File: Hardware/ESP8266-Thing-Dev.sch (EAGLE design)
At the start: 83 parts, among them J1 DNP, Q1 MMBT2222A, Q2 MMBT2222A, Q4 BSS138, Q5 BSS138, Q6 BSS138, Q7 BSS138, Q8 BSS138, U1 AP2112K-3.3V, U2 ESP8266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

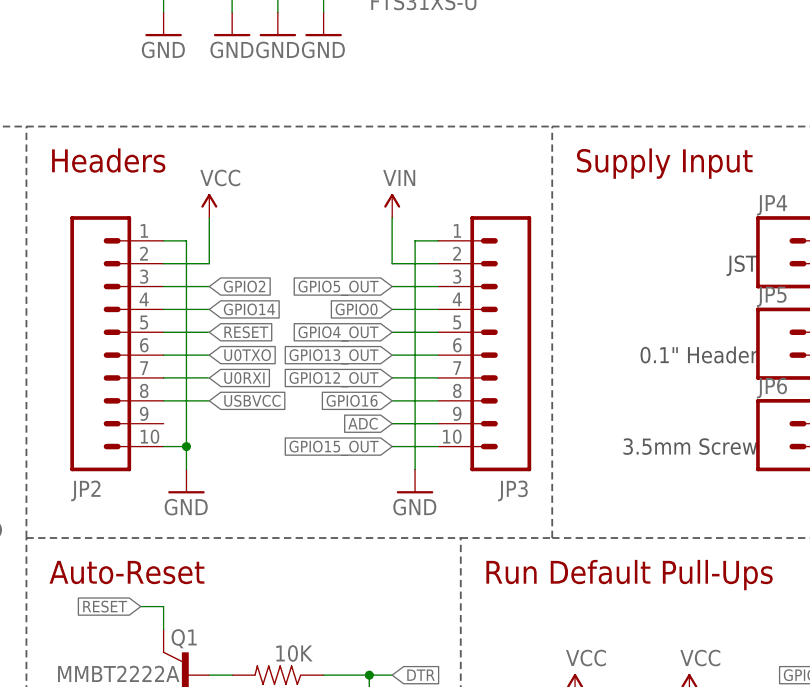
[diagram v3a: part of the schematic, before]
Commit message: Switch to 7 pin header. Make board outline larger.
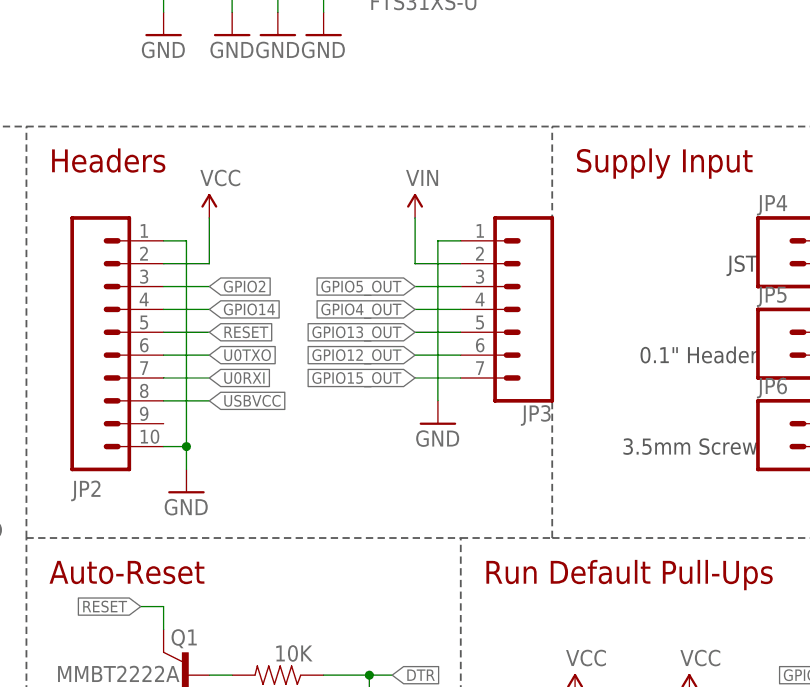
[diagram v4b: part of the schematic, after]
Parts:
- JP3: device SparkFun-Connectors:M10NO_SILK_PTH_FEMALE -> SparkFun-Connectors:CONN_07NO_SILK
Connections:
- net ADC: no longer JP3.9
- net GPIO0: no longer JP3.4
- net GPIO12_OUT: now also JP3.6; no longer JP3.7
- net GPIO13_OUT: now also JP3.5; no longer JP3.6
- net GPIO15_OUT: now also JP3.7; no longer JP3.10
- net GPIO16: no longer JP3.8
- net GPIO4_OUT: now also JP3.4; no longer JP3.5
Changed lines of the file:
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@@
 <layer number="112" name="tSilk" color="7" fill="1" visible="yes" active="yes"/>
 <layer number="113" name="IDFDebug" color="4" fill="1" visible="yes" active="yes"/>
+<layer number="114" name="Badge_Outline" color="7" fill="1" visible="yes" active="yes"/>
+<layer number="115" name="ReferenceISLANDS" color="7" fill="1" visible="yes" active="yes"/>
 <layer number="116" name="Patch_BOT" color="9" fill="4" visible="yes" active="yes"/>
 <layer number="118" name="Rect_Pads" color="7" fill="1" visible="yes" active="yes"/>
@@
 <layer number="230" name="230bmp" color="7" fill="1" visible="yes" active="yes"/>
 <layer number="231" name="231bmp" color="7" fill="1" visible="yes" active="yes"/>
+<layer number="232" name="Eagle3D_PG2" color="7" fill="1" visible="yes" active="yes"/>
+<layer number="233" name="Eagle3D_PG3" color="7" fill="1" visible="yes" active="yes"/>
 <layer number="248" name="Housing" color="7" fill="1" visible="yes" active="yes"/>
 <layer number="249" name="Edge" color="7" fill="1" visible="yes" active="yes"/>
@@
 <part name="SJ2" library="SparkFun-Passives" deviceset="JUMPER-PTH-2-NO" device="" value="SLEEP-PTH"/>
 <part name="JP2" library="SparkFun-Connectors" deviceset="M10" device="NO_SILK_PTH_FEMALE"/>
-<part name="JP3" library="SparkFun-Connectors" deviceset="M10" device="NO_SILK_PTH_FEMALE"/>
 <part name="STANDOFF3" library="SparkFun-Electromechanical" deviceset="STAND-OFF" device=""/>
 <part name="STANDOFF1" library="SparkFun-Electromechanical" deviceset="STAND-OFF" device=""/>
@@
 <part name="R28" library="SparkFun" deviceset="RESISTOR" device="0603-RES" value="10K"/>
 <part name="R29" library="SparkFun" deviceset="RESISTOR" device="0603-RES" value="10K"/>
+<part name="JP3" library="SparkFun-Connectors" library_urn="urn:adsk.eagle:library:513" deviceset="CONN_07" device="NO_SILK" package3d_urn="urn:adsk.eagle:package:38136/1"/>
 </parts>
 <sheets>
@@
 </instance>
 <instance part="JP2" gate="G$1" x="152.4" y="93.98" rot="MR180"/>
-<instance part="JP3" gate="G$1" x="203.2" y="93.98" rot="R180"/>
 <instance part="STANDOFF3" gate="G$1" x="246.38" y="33.02"/>
 <instance part="STANDOFF1" gate="G$1" x="243.84" y="33.02"/>
@@
 <instance part="SUPPLY10" gate="G$1" x="167.64" y="114.3"/>
 <instance part="GND22" gate="1" x="165.1" y="83.82"/>
-<instance part="SUPPLY11" gate="G$1" x="187.96" y="114.3"/>
-<instance part="GND26" gate="1" x="190.5" y="83.82"/>
+<instance part="SUPPLY11" gate="G$1" x="190.5" y="114.3"/>
+<instance part="GND26" gate="1" x="193.04" y="91.44"/>
 <instance part="J1" gate="G$1" x="137.16" y="93.98" smashed="yes" rot="MR0">
 <attribute name="NAME" x="140.97" y="98.044" size="1.778" layer="95" rot="MR0"/>
@@
 <instance part="R28" gate="G$1" x="269.24" y="17.78" rot="R270"/>
 <instance part="R29" gate="G$1" x="284.48" y="17.78" rot="R270"/>
+<instance part="JP3" gate="G$1" x="200.66" y="106.68" rot="R180"/>
 </instances>
 <busses>
@@
 </segment>
 <segment>
+<wire x1="195.58" y1="111.76" x2="193.04" y2="111.76" width="0.1524" layer="91"/>
+<wire x1="193.04" y1="111.76" x2="193.04" y2="93.98" width="0.1524" layer="91"/>
+<pinref part="GND26" gate="1" pin="GND"/>
 <pinref part="JP3" gate="G$1" pin="1"/>
-<wire x1="193.04" y1="111.76" x2="190.5" y2="111.76" width="0.1524" layer="91"/>
-<wire x1="190.5" y1="111.76" x2="190.5" y2="86.36" width="0.1524" layer="91"/>
-<pinref part="GND26" gate="1" pin="GND"/>
 </segment>
 <segment>
@@
 <label x="73.66" y="33.02" size="1.27" layer="95" xref="yes"/>
 </segment>
-<segment>
-<pinref part="JP3" gate="G$1" pin="9"/>
-<wire x1="193.04" y1="91.44" x2="187.96" y2="91.44" width="0.1524" layer="91"/>
-<label x="187.96" y="91.44" size="1.27" layer="95" rot="R180" xref="yes"/>
-</segment>
 </net>
 <net name="GPIO0" class="0">
@@
 <wire x1="162.56" y1="38.1" x2="160.02" y2="38.1" width="0.1524" layer="91"/>
 <label x="160.02" y="38.1" size="1.27" layer="95" rot="R180" xref="yes"/>
-</segment>
-<segment>
-<pinref part="JP3" gate="G$1" pin="4"/>
-<wire x1="193.04" y1="104.14" x2="187.96" y2="104.14" width="0.1524" layer="91"/>
-<label x="187.96" y="104.14" size="1.27" layer="95" rot="R180" xref="yes"/>
 </segment>
 </net>
@@
 <wire x1="73.66" y1="35.56" x2="76.2" y2="35.56" width="0.1524" layer="91" style="longdash"/>
 <label x="76.2" y="35.56" size="1.27" layer="95" xref="yes"/>
-</segment>
-<segment>
-<pinref part="JP3" gate="G$1" pin="8"/>
-<wire x1="193.04" y1="93.98" x2="187.96" y2="93.98" width="0.1524" layer="91"/>
-<label x="187.96" y="93.98" size="1.27" layer="95" rot="R180" xref="yes"/>
 </segment>
 </net>
@@
 </segment>
 <segment>
+<wire x1="195.58" y1="109.22" x2="190.5" y2="109.22" width="0.1524" layer="91"/>
+<wire x1="190.5" y1="109.22" x2="190.5" y2="114.3" width="0.1524" layer="91"/>
+<pinref part="SUPPLY11" gate="G$1" pin="VIN"/>
 <pinref part="JP3" gate="G$1" pin="2"/>
-<wire x1="193.04" y1="109.22" x2="187.96" y2="109.22" width="0.1524" layer="91"/>
-<wire x1="187.96" y1="109.22" x2="187.96" y2="114.3" width="0.1524" layer="91"/>
-<pinref part="SUPPLY11" gate="G$1" pin="VIN"/>
 </segment>
 <segment>
@@
 </segment>
 <segment>
+<wire x1="195.58" y1="106.68" x2="190.5" y2="106.68" width="0.1524" layer="91"/>
+<label x="190.5" y="106.68" size="1.27" layer="95" rot="R180" xref="yes"/>
 <pinref part="JP3" gate="G$1" pin="3"/>
-<wire x1="193.04" y1="106.68" x2="187.96" y2="106.68" width="0.1524" layer="91"/>
-<label x="187.96" y="106.68" size="1.27" layer="95" rot="R180" xref="yes"/>
 </segment>
 </net>
@@
 </segment>
 <segment>
-<pinref part="JP3" gate="G$1" pin="6"/>
-<wire x1="193.04" y1="99.06" x2="187.96" y2="99.06" width="0.1524" layer="91"/>
-<label x="187.96" y="99.06" size="1.27" layer="95" rot="R180" xref="yes"/>
+<wire x1="195.58" y1="101.6" x2="190.5" y2="101.6" width="0.1524" layer="91"/>
+<label x="190.5" y="101.6" size="1.27" layer="95" rot="R180" xref="yes"/>
+<pinref part="JP3" gate="G$1" pin="5"/>
 </segment>
 </net>
@@
 </segment>
 <segment>
-<pinref part="JP3" gate="G$1" pin="7"/>
-<wire x1="193.04" y1="96.52" x2="187.96" y2="96.52" width="0.1524" layer="91"/>
-<label x="187.96" y="96.52" size="1.27" layer="95" rot="R180" xref="yes"/>
+<wire x1="195.58" y1="99.06" x2="190.5" y2="99.06" width="0.1524" layer="91"/>
+<label x="190.5" y="99.06" size="1.27" layer="95" rot="R180" xref="yes"/>
+<pinref part="JP3" gate="G$1" pin="6"/>
 </segment>
 </net>
@@
 </segment>
 <segment>
-<pinref part="JP3" gate="G$1" pin="5"/>
-<wire x1="193.04" y1="101.6" x2="187.96" y2="101.6" width="0.1524" layer="91"/>
-<label x="187.96" y="101.6" size="1.27" layer="95" rot="R180" xref="yes"/>
+<wire x1="195.58" y1="104.14" x2="190.5" y2="104.14" width="0.1524" layer="91"/>
+<label x="190.5" y="104.14" size="1.27" layer="95" rot="R180" xref="yes"/>
+<pinref part="JP3" gate="G$1" pin="4"/>
 </segment>
 </net>
 <net name="GPIO15_OUT" class="0">
 <segment>
-<pinref part="JP3" gate="G$1" pin="10"/>
-<wire x1="193.04" y1="88.9" x2="187.96" y2="88.9" width="0.1524" layer="91"/>
-<label x="187.96" y="88.9" size="1.27" layer="95" rot="R180" xref="yes"/>
+<wire x1="195.58" y1="96.52" x2="190.5" y2="96.52" width="0.1524" layer="91"/>
+<label x="190.5" y="96.52" size="1.27" layer="95" rot="R180" xref="yes"/>
+<pinref part="JP3" gate="G$1" pin="7"/>
 </segment>
 <segment>
@@
 which will not be processed correctly with this version.
 </note>
+<note version="8.2" severity="warning">
+Since Version 8.2, EAGLE supports online libraries. The ids
+of those online libraries will not be understood (or retained)
+with this version.
+</note>
+<note version="8.3" severity="warning">
+Since Version 8.3, EAGLE supports URNs for individual library
+assets (packages, symbols, and devices). The URNs of those assets
+will not be understood (or retained) with this version.
+</note>
+<note version="8.3" severity="warning">
+Since Version 8.3, EAGLE supports the association of 3D packages
+with devices in libraries, schematics, and board files. Those 3D
+packages will not be understood (or retained) with this version.
+</note>
 </compatibility>
